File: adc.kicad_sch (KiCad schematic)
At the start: 5 parts, among them U6 ADS1115IDGSR

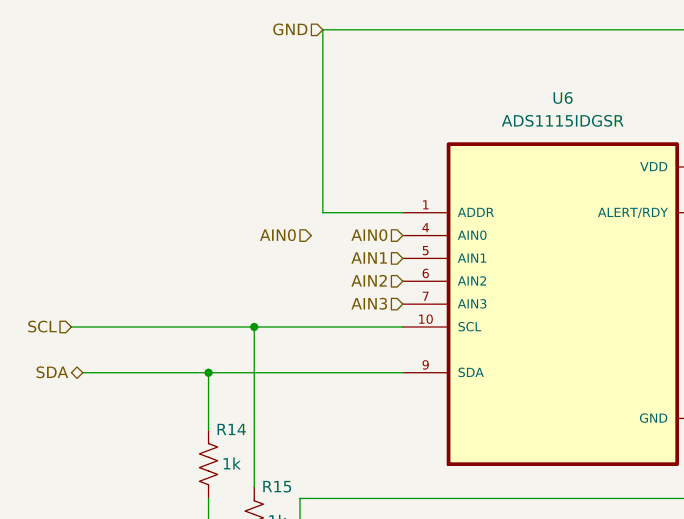
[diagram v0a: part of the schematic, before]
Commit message: Filter abstraction and Input output connectors
Abstracted filters so there are 4 signal paths to go to ADC. Added input and output connectors.
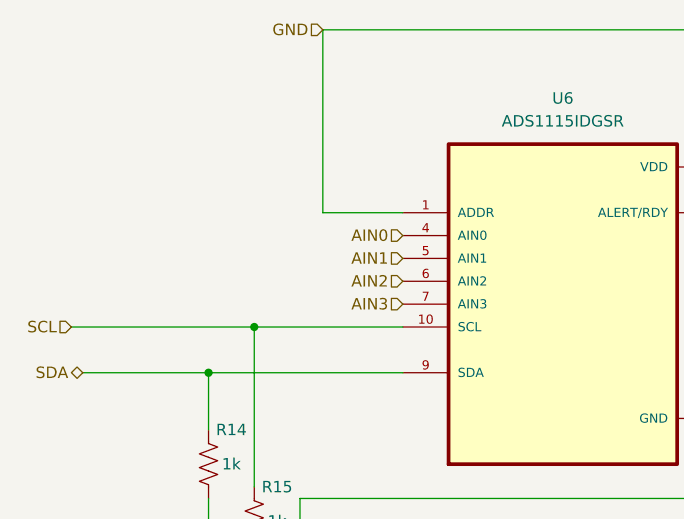
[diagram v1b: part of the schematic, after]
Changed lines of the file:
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@@
-    (effects (font (size 1.27 1.27)) (justify right))
-  )
-  (hierarchical_label "AIN0" (shape input) (at 101.6 78.74 180) (fields_autoplaced)
     (effects (font (size 1.27 1.27)) (justify right))
   )

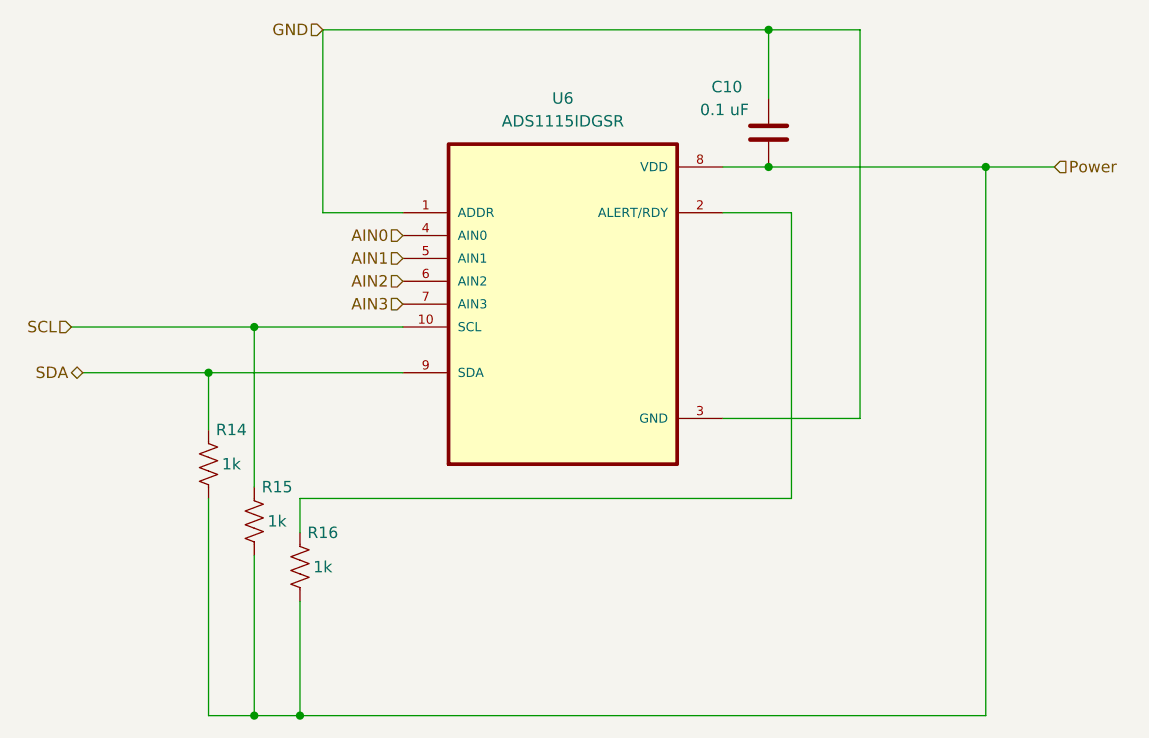
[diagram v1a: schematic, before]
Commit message: removed sda scl pullups, removed electrode connectors to make space for proper connectors later
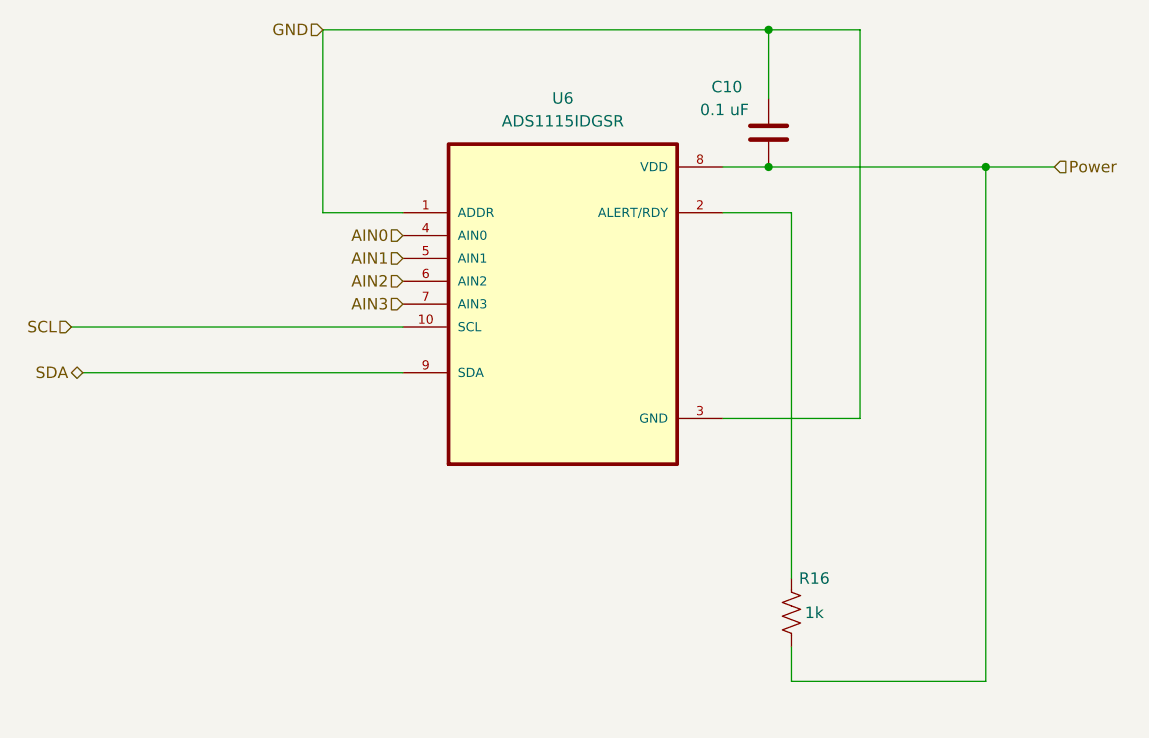
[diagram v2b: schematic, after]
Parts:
- removed R14, R15: 1k, symbol Device:R_US
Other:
- moved on the sheet: R16
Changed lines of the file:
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@@
   (junction (at 152.4 71.12) (diameter 0) (color 0 0 0 0)
-  )
-  (junction (at 90.17 93.98) (diameter 0) (color 0 0 0 0)
-  )
-  (junction (at 95.25 88.9) (diameter 0) (color 0 0 0 0)
   )
   (junction (at 152.4 55.88) (diameter 0) (color 0 0 0 0)
   )
-  (junction (at 100.33 132.08) (diameter 0) (color 0 0 0 0)
-  )
-  (junction (at 95.25 132.08) (diameter 0) (color 0 0 0 0)
-  )
-  (wire (pts (xy 76.2 93.98) (xy 90.17 93.98))
+  (wire (pts (xy 76.2 93.98) (xy 111.76 93.98))
     (stroke (width 0) (type default))
   )
@@
     (stroke (width 0) (type default))
   )
-  (wire (pts (xy 90.17 107.95) (xy 90.17 132.08))
-    (stroke (width 0) (type default))
-  )
-  (wire (pts (xy 176.53 71.12) (xy 176.53 132.08))
+  (wire (pts (xy 176.53 71.12) (xy 176.53 128.27))
     (stroke (width 0) (type default))
   )
@@
     (stroke (width 0) (type default))
   )
-  (wire (pts (xy 74.93 88.9) (xy 95.25 88.9))
+  (wire (pts (xy 74.93 88.9) (xy 111.76 88.9))
     (stroke (width 0) (type default))
   )
-  (wire (pts (xy 100.33 132.08) (xy 100.33 119.38))
+  (wire (pts (xy 154.94 128.27) (xy 154.94 124.46))
     (stroke (width 0) (type default))
   )
-  (wire (pts (xy 154.94 76.2) (xy 154.94 107.95))
+  (wire (pts (xy 154.94 76.2) (xy 154.94 116.84))
     (stroke (width 0) (type default))
   )
   (wire (pts (xy 162.56 99.06) (xy 162.56 55.88))
-    (stroke (width 0) (type default))
-  )
-  (wire (pts (xy 95.25 132.08) (xy 100.33 132.08))
     (stroke (width 0) (type default))
   )
@@
     (stroke (width 0) (type default))
   )
-  (wire (pts (xy 90.17 93.98) (xy 111.76 93.98))
-    (stroke (width 0) (type default))
-  )
-  (wire (pts (xy 176.53 132.08) (xy 100.33 132.08))
+  (wire (pts (xy 176.53 128.27) (xy 154.94 128.27))
     (stroke (width 0) (type default))
   )
@@
     (stroke (width 0) (type default))
   )
-  (wire (pts (xy 95.25 88.9) (xy 95.25 106.68))
-    (stroke (width 0) (type default))
-  )
   (wire (pts (xy 162.56 55.88) (xy 152.4 55.88))
-    (stroke (width 0) (type default))
-  )
-  (wire (pts (xy 90.17 93.98) (xy 90.17 100.33))
-    (stroke (width 0) (type default))
-  )
-  (wire (pts (xy 90.17 132.08) (xy 95.25 132.08))
     (stroke (width 0) (type default))
   )
@@
     (stroke (width 0) (type default))
   )
-  (wire (pts (xy 95.25 114.3) (xy 95.25 132.08))
-    (stroke (width 0) (type default))
-  )
-  (wire (pts (xy 154.94 107.95) (xy 100.33 107.95))
-    (stroke (width 0) (type default))
-  )
   (wire (pts (xy 184.15 71.12) (xy 176.53 71.12))
-    (stroke (width 0) (type default))
-  )
-  (wire (pts (xy 95.25 88.9) (xy 111.76 88.9))
-    (stroke (width 0) (type default))
-  )
-  (wire (pts (xy 100.33 107.95) (xy 100.33 111.76))
     (stroke (width 0) (type default))
   )
@@
     )
   )
-  (symbol (lib_id "Device:R_US") (at 100.33 115.57 180) (unit 1)
+  (symbol (lib_id "Device:R_US") (at 154.94 120.65 180) (unit 1)
     (in_bom yes) (on_board yes) (dnp no)
-    (property "Reference" "R16" (at 102.87 111.76 0)
+    (property "Reference" "R16" (at 157.48 116.84 0)
       (effects (font (size 1.27 1.27)))
     )
-    (property "Value" "1k" (at 102.87 115.57 0)
+    (property "Value" "1k" (at 157.48 120.65 0)
       (effects (font (size 1.27 1.27)))
     )
-    (property "Footprint" "" (at 99.314 115.316 90)
+    (property "Footprint" "" (at 153.924 120.396 90)
       (effects (font (size 1.27 1.27)) hide)
     )
-    (property "Datasheet" "~" (at 100.33 115.57 0)
+    (property "Datasheet" "~" (at 154.94 120.65 0)
       (effects (font (size 1.27 1.27)) hide)
     )
@@
         )
       )
-    )
-  )
-  (symbol (lib_id "Device:R_US") (at 90.17 104.14 180) (unit 1)
-    (in_bom yes) (on_board yes) (dnp no)
-    (property "Reference" "R14" (at 92.71 100.33 0)
-      (effects (font (size 1.27 1.27)))
-    )
-    (property "Value" "1k" (at 92.71 104.14 0)
-      (effects (font (size 1.27 1.27)))
-    )
-    (property "Footprint" "" (at 89.154 103.886 90)
-      (effects (font (size 1.27 1.27)) hide)
-    )
-    (property "Datasheet" "~" (at 90.17 104.14 0)
-      (effects (font (size 1.27 1.27)) hide)
-    )
-    (pin "1")
-    (pin "2")
-    (instances
-      (project "TR_EMG"
-        (path "/c6167f6f-8a8c-40a1-9c06-7f0e8ea44639/c018842c-498f-47c8-a015-784e87d3039e"
-          (reference "R14") (unit 1)
-        )
-      )
-    )
-  )
-  (symbol (lib_id "Device:R_US") (at 95.25 110.49 180) (unit 1)
-    (in_bom yes) (on_board yes) (dnp no)
-    (property "Reference" "R15" (at 97.79 106.68 0)
-      (effects (font (size 1.27 1.27)))
-    )
-    (property "Value" "1k" (at 97.79 110.49 0)
-      (effects (font (size 1.27 1.27)))
-    )
-    (property "Footprint" "" (at 94.234 110.236 90)
-      (effects (font (size 1.27 1.27)) hide)
-    )
-    (property "Datasheet" "~" (at 95.25 110.49 0)
-      (effects (font (size 1.27 1.27)) hide)
-    )
-    (pin "1")
-    (pin "2")
-    (instances
-      (project "TR_EMG"
-        (path "/c6167f6f-8a8c-40a1-9c06-7f0e8ea44639/c018842c-498f-47c8-a015-784e87d3039e"
-          (reference "R15") (unit 1)
-        )
-      )

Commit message: Reference Designator and Footprint Updates
Changed almost all reference designators to group similar components by what filter they are a part of and what value they have.

Need to:
- Sort symbol data for ADC and OpAmps to correct folders
- get footprint files for ADC and OpAmps
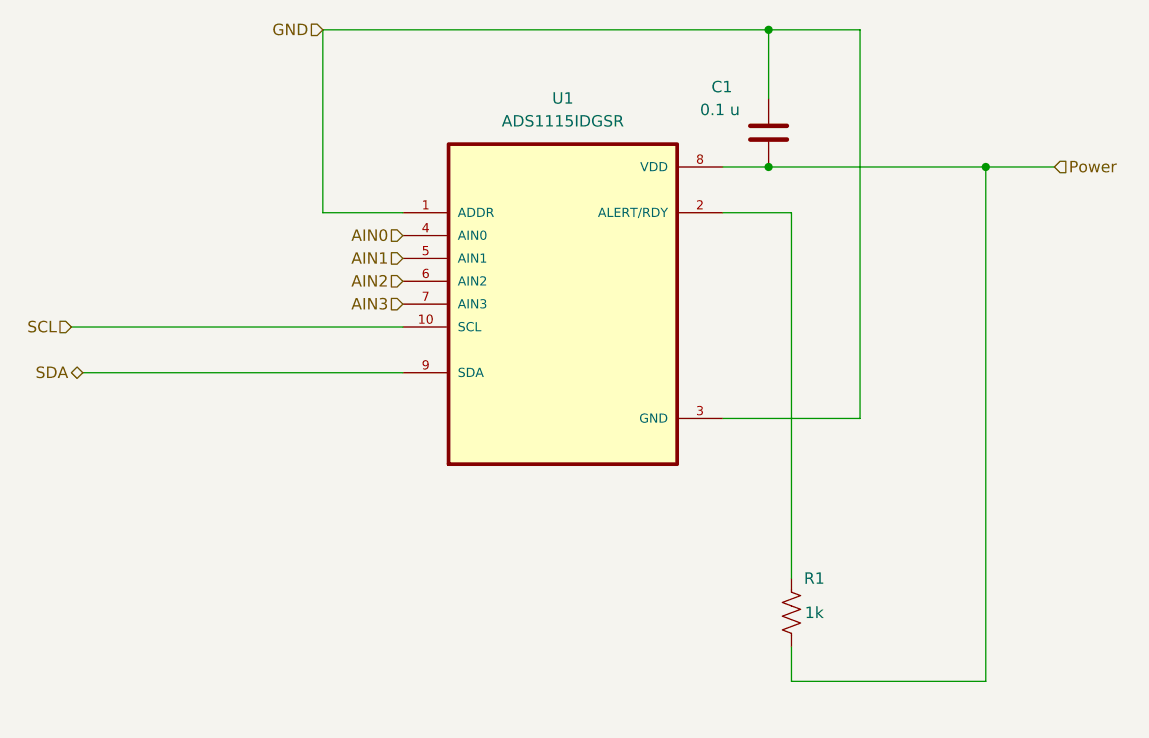
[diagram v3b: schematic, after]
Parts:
- C1: renamed from C10; value 0.1 uF -> 0.1 u; footprint (none) -> Capacitor_SMD:C_0603_1608Metric_Pad1.08x0.95mm_HandSolder
- R1: renamed from R16; footprint (none) -> Resistor_SMD:R_0603_1608Metric_Pad0.98x0.95mm_HandSolder
- renumbered U6 to U1
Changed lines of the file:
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@@
   (symbol (lib_id "symbols:ADS1115IDGSR") (at 129.54 86.36 0) (unit 1)
     (in_bom yes) (on_board yes) (dnp no) (fields_autoplaced)
-    (property "Reference" "U6" (at 129.54 63.5 0)
+    (property "Reference" "U1" (at 129.54 63.5 0)
       (effects (font (size 1.27 1.27)))
     )
@@
       (project "TR_EMG"
         (path "/c6167f6f-8a8c-40a1-9c06-7f0e8ea44639/c018842c-498f-47c8-a015-784e87d3039e"
-          (reference "U6") (unit 1)
+          (reference "U1") (unit 1)
         )
       )
@@
   (symbol (lib_id "Device:R_US") (at 154.94 120.65 180) (unit 1)
     (in_bom yes) (on_board yes) (dnp no)
-    (property "Reference" "R16" (at 157.48 116.84 0)
+    (property "Reference" "R1" (at 157.48 116.84 0)
       (effects (font (size 1.27 1.27)))
     )
@@
       (effects (font (size 1.27 1.27)))
     )
-    (property "Footprint" "" (at 153.924 120.396 90)
+    (property "Footprint" "Resistor_SMD:R_0603_1608Metric_Pad0.98x0.95mm_HandSolder" (at 153.924 120.396 90)
       (effects (font (size 1.27 1.27)) hide)
     )
@@
       (project "TR_EMG"
         (path "/c6167f6f-8a8c-40a1-9c06-7f0e8ea44639/c018842c-498f-47c8-a015-784e87d3039e"
-          (reference "R16") (unit 1)
+          (reference "R1") (unit 1)
         )
       )
@@
   (symbol (lib_id "Device:C") (at 152.4 67.31 0) (unit 1)
     (in_bom yes) (on_board yes) (dnp no)
-    (property "Reference" "C10" (at 146.05 62.23 0)
+    (property "Reference" "C1" (at 146.05 62.23 0)
       (effects (font (size 1.27 1.27)) (justify left))
     )
-    (property "Value" "0.1 uF" (at 144.78 64.77 0)
+    (property "Value" "0.1 u" (at 144.78 64.77 0)
       (effects (font (size 1.27 1.27)) (justify left))
     )
-    (property "Footprint" "" (at 153.3652 71.12 0)
+    (property "Footprint" "Capacitor_SMD:C_0603_1608Metric_Pad1.08x0.95mm_HandSolder" (at 153.3652 71.12 0)
       (effects (font (size 1.27 1.27)) hide)
     )
@@
       (project "TR_EMG"
         (path "/c6167f6f-8a8c-40a1-9c06-7f0e8ea44639/c018842c-498f-47c8-a015-784e87d3039e"
-          (reference "C10") (unit 1)
+          (reference "C1") (unit 1)
         )
       )

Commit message: renamed and relinked footprints with better clarity footprint file names
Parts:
- U1: footprint ADS1115IDGSR:SOP50P490X110-10N -> footprints:ADS-SOP50P490X110-10N
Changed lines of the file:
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@@
       (effects (font (size 1.27 1.27)))
     )
-    (property "Footprint" "ADS1115IDGSR:SOP50P490X110-10N" (at 129.54 86.36 0)
+    (property "Footprint" "footprints:ADS-SOP50P490X110-10N" (at 129.54 86.36 0)
       (effects (font (size 1.27 1.27)) (justify bottom) hide)
     )

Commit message: changed capacitor footprint to match in stock components (0603 to 1206)
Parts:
- C1: footprint Capacitor_SMD:C_0603_1608Metric_Pad1.08x0.95mm_HandSolder -> Capacitor_SMD:C_1206_3216Metric
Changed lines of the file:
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@@
       (effects (font (size 1.27 1.27)) (justify left))
     )
-    (property "Footprint" "Capacitor_SMD:C_0603_1608Metric_Pad1.08x0.95mm_HandSolder" (at 153.3652 71.12 0)
+    (property "Footprint" "Capacitor_SMD:C_1206_3216Metric" (at 153.3652 71.12 0)
       (effects (font (size 1.27 1.27)) hide)
     )

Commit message: ToTheEdge,LCSCNums
Moved the 3.5mm connectors to the edge and edited their footprint courtyard so no errors. Adjusted the planes so that it bordered 3.5mm connector pads well and didn't go to edge cuts. Added LCSC part numbers to the parts that were in stock.
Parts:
- C1: LCSC (none) -> C2981728
- R1: LCSC (none) -> C705913
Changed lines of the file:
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@@
+      (effects (font (size 1.27 1.27)) hide)
+    )
+    (property "LCSC" "" (at 129.54 86.36 0)
       (effects (font (size 1.27 1.27)) hide)
     )
@@
       (effects (font (size 1.27 1.27)) hide)
     )
+    (property "LCSC" "C705913" (at 154.94 120.65 0)
+      (effects (font (size 1.27 1.27)) hide)
+    )
     (pin "1")
     (pin "2")
@@
       (effects (font (size 1.27 1.27)) hide)
     )
+    (property "LCSC" "C2981728" (at 152.4 67.31 0)
+      (effects (font (size 1.27 1.27)) hide)
+    )
